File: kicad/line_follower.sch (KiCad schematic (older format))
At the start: 40 parts, among them Q1 ALS-PT19-315C_L177_TR8, Q2 ALS-PT19-315C_L177_TR8, Q3 ALS-PT19-315C_L177_TR8, Q4 ALS-PT19-315C_L177_TR8, Q5 ALS-PT19-315C_L177_TR8, SW1 SW_Push, U1 A4950E, U2 A4950E, U3 NCV4274CDT50RKG, X1 ESP32_DEVKITV1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

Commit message: Board: Almost complete schematic, rough layout of pcb
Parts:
- removed Q1, Q2, Q3, Q4, Q5: ALS-PT19-315C_L177_TR8, line_follower:PHOTOTRANSISTOR-1.7MM, symbol line_follower-eagle-import:ALS-PT19-315C_L177_TR8
- added Q2, Q3, Q4, Q5: ALS-PT19-315C_L177_TR8, cube-library:phototransistor-1.7mm, symbol Device:Q_Photo_NPN
- C8, C9: renamed from C?; footprint (none) -> Capacitor_SMD:CP_Elec_6.3x5.8
- M1, M2: renamed from M?; footprint (none) -> cube-library:SolderWirePad1x6_p2.54
- Q1: renamed from Q?; value Q_Photo_NPN -> ALS-PT19-315C_L177_TR8; footprint (none) -> cube-library:phototransistor-1.7mm
- SW1: footprint (none) -> cube-library:4.5mm_tact_switch
- U1, U2: footprint Package_SO:SOIC-8-1EP_3.9x4.9mm_P1.27mm_EP2.41x3.3mm -> cube-library:SOIC-8-1EP_3.9x4.9mm_P1.27mm_EP2.41x3.3mm_HandSolder
- X1: footprint esp32_devkitv1:ESP32_DEVKITV1 -> cube-library:ESP32_DEVKITV1
- X3: footprint (none) -> cube-library:SolderWirePad1x3_p2.54
- gave numbers to parts that had none: 14
- renumbered R1 to R6, R2 to R7
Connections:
- net labels removed: VBAT
- no-connect marks 0 -> 7
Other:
- note added: "EN has internal pull up"
- note added: "Line sensor LEDs\n\nCharlieplexing leds, using ESP32 GPIO drive strength to limit current.\nShould be safe even at max drive strength at about 30mA per LED.\n\nSee https://www.esp32.com/viewtopic.php?f=12&t=5840#p25550"
- note added: "Power supply:\n\nBoth ESP32-DEVKITV1 and GY-521 have on board 3.3V regulators.\nWe're using the one on ESP32 to power small stuff around the board.\n\nNCV4274CDT low dropout voltage regulator was chosen because it\nhas low enough dropout voltage to power the board from 2S LiPo,\nand has an internal diode in series, so that back powering the board\nfrom USB is safe (Powers everything except the mo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"
- note added: "Secondary I2C is not used"
- note removed: "Line sensor LEDs\n\nCharlieplexing leds, using ESP32 GPIO drive strength to limit current.\nShould be fairly safe even at max drive strength at about 30mA per LED.\n\nSee https://www.esp32.com/viewtopic.php?f=12&t=5840#p25550"
- note removed: "Power supply:\n\nBoth ESP32-DEVKITV1 and GY-521 have on board 3.3V regulators.\nWe're using the one on ESP32 to power small stuff around the board."
- moved on the sheet: C1, C10, C11, C2, C3, C4, C5, C6, C7, C8, C9, D1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

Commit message: Getting there with the PCB design.
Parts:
- added HS1, HS2, HS3, HS4: Heatsink_Pad, cube-library:3x3_thermal_vias, symbol Mechanical:Heatsink_Pad
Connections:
- net +3V3: now also U1.4 (VREF), U2.4 (VREF)
- net +5V: no longer U1.4 (VREF), U2.4 (VREF)
- net ENCODER1A: now also X1.21 (RX2); no longer X1.3 (VN)
- net ENCODER1B: now also X1.22 (TX2); no longer X1.2 (VP)
- net ENCODER2A: now also X1.2 (VP); no longer X1.22 (TX2)
- net ENCODER2B: now also X1.3 (VN); no longer X1.21 (RX2)
- net GND: now also HS1.1, HS2.1, HS3.1, HS4.1
- net LINE_LED0: now also X1.10 (D27); no longer X1.8 (D25)
- net LINE_LED1: now also X1.8 (D25); no longer X1.9 (D26)
- net LINE_LED2: now also X1.9 (D26); no longer X1.10 (D27)
- net LINE_SENSOR0: now also X1.7 (D33); no longer X1.4 (D34)
- net LINE_SENSOR3: now also X1.5 (D35); no longer X1.11 (D14)
- net LINE_SENSOR4: now also X1.4 (D34); no longer X1.7 (D33)
- net MOTOR1A: now also X1.13 (D13); no longer X1.25 (D19)
- net MOTOR1B: now also X1.12 (D12); no longer X1.30 (D23)
- net MOTOR2A: now also X1.30 (D23); no longer X1.12 (D12)
- net MOTOR2B: now also X1.25 (D19); no longer X1.13 (D13)
- net RANGE: now also X1.11 (D14); no longer X1.5 (D35)
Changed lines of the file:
@@
 	550  1450 1350 1450
 Text Label 550  1450 0    70   ~ 0
-LINE_LED0
+LINE_LED1
 Wire Wire Line
 	1350 1550 550  1550
 Text Label 550  1550 0    70   ~ 0
-LINE_LED1
+LINE_LED2
 Wire Wire Line
 	1350 1650 550  1650
 Text Label 550  1650 0    70   ~ 0
-LINE_LED2
+LINE_LED0
 Wire Wire Line
 	1350 1850 550  1850
 Text Label 550  1850 0    70   ~ 0
-MOTOR2A
+MOTOR1B
 Wire Wire Line
 	2450 2150 2550 2150
@@
 	1350 1950 550  1950
 Text Label 550  1950 0    70   ~ 0
-MOTOR2B
+MOTOR1A
 Wire Wire Line
 	2450 750  3250 750
 Text Label 3250 750  2    70   ~ 0
-MOTOR1B
+MOTOR2A
 Wire Wire Line
 	2450 1250 3250 1250
 Text Label 3250 1250 2    70   ~ 0
-MOTOR1A
+MOTOR2B
 Text Label 1000 4700 0    70   ~ 0
 BUTTON
@@
 	1350 1150 550  1150
 Text Label 550  1150 0    70   ~ 0
-RANGE
+LINE_SENSOR3
 Wire Wire Line
 	1000 7000 1200 7000
@@
 	550  1350 1350 1350
 Text Label 550  1350 0    70   ~ 0
-LINE_SENSOR4
+LINE_SENSOR0
 Wire Wire Line
 	550  1750 1350 1750
 Text Label 550  1750 0    70   ~ 0
-LINE_SENSOR3
+RANGE
 Wire Wire Line
 	550  1250 1350 1250
@@
 	550  1050 1350 1050
 Text Label 550  1050 0    70   ~ 0
-LINE_SENSOR0
+LINE_SENSOR4
 Wire Wire Line
 	1350 850  550  850
 Text Label 550  850  0    70   ~ 0
-ENCODER1B
+ENCODER2A
 Wire Wire Line
 	1350 950  550  950
 Text Label 550  950  0    70   ~ 0
-ENCODER1A
+ENCODER2B
 Wire Wire Line
 	2450 1550 3250 1550
 Text Label 3250 1550 2    70   ~ 0
-ENCODER2A
+ENCODER1B
 Wire Wire Line
 	2450 1650 3250 1650
 Text Label 3250 1650 2    70   ~ 0
-ENCODER2B
+ENCODER1A
 Wire Wire Line
 	1500 3200 800  3200
@@
 $EndComp
 $Comp
-L power:+5V #PWR0104
-U 1 1 5F6B266B
-P 4750 6950
-F 0 "#PWR0104" H 4750 6800 50  0001 C CNN
-F 1 "+5V" V 4765 7078 50  0000 L CNN
-F 2 "" H 4750 6950 50  0001 C CNN
-F 3 "" H 4750 6950 50  0001 C CNN
-	1    4750 6950
-	0    -1   -1   0
-$EndComp
-$Comp
 L cube-library:MOTOR_ENC M2
 U 1 1 5F092189
@@
 $EndComp
 $Comp
-L power:+5V #PWR0103
-U 1 1 5F6B001E
-P 4750 4250
-F 0 "#PWR0103" H 4750 4100 50  0001 C CNN
-F 1 "+5V" V 4765 4378 50  0000 L CNN
-F 2 "" H 4750 4250 50  0001 C CNN
-F 3 "" H 4750 4250 50  0001 C CNN
-	1    4750 4250
-	0    -1   -1   0
-$EndComp
-$Comp
 L cube-library:MOTOR_ENC M1
 U 1 1 5F08FA5D
@@
 Wire Wire Line
 	5250 4650 5250 4800
-Wire Wire Line
-	5250 4650 5250 4550
 Connection ~ 5250 4650
 Wire Wire Line
@@
 Wire Wire Line
 	9850 4200 10050 4200
+$Comp
+L Mechanical:Heatsink_Pad HS1
+U 1 1 5F1F9B2A
+P 6750 3050
+F 0 "HS1" H 6891 3089 50  0000 L CNN
+F 1 "Heatsink_Pad" H 6891 2998 50  0000 L CNN
+F 2 "cube-library:3x3_thermal_vias" H 6762 3000 50  0001 C CNN
+F 3 "~" H 6762 3000 50  0001 C CNN
+	1    6750 3050
+	1    0    0    -1
+$EndComp
+$Comp
+L Mechanical:Heatsink_Pad HS2
+U 1 1 5F204F60
+P 6750 3550
+F 0 "HS2" H 6891 3589 50  0000 L CNN
+F 1 "Heatsink_Pad" H 6891 3498 50  0000 L CNN
+F 2 "cube-library:3x3_thermal_vias" H 6762 3500 50  0001 C CNN
+F 3 "~" H 6762 3500 50  0001 C CNN
+	1    6750 3550
+	1    0    0    -1
+$EndComp
+Wire Wire Line
+	5250 4650 5250 4550
+$Comp
+L power:GND #PWR0127
+U 1 1 5F2722C1
+P 6750 3150
+F 0 "#PWR0127" H 6750 2900 50  0001 C CNN
+F 1 "GND" H 6755 2977 50  0000 C CNN
+F 2 "" H 6750 3150 50  0001 C CNN
+F 3 "" H 6750 3150 50  0001 C CNN
+	1    6750 3150
+	1    0    0    -1
+$EndComp
+$Comp
+L power:GND #PWR0128
+U 1 1 5F27922E
+P 6750 3650
+F 0 "#PWR0128" H 6750 3400 50  0001 C CNN
+F 1 "GND" H 6755 3477 50  0000 C CNN
+F 2 "" H 6750 3650 50  0001 C CNN
+F 3 "" H 6750 3650 50  0001 C CNN
+	1    6750 3650
+	1    0    0    -1
+$EndComp
+$Comp
+L Mechanical:Heatsink_Pad HS3
+U 1 1 5F292D49
+P 6700 5750
+F 0 "HS3" H 6841 5789 50  0000 L CNN
+F 1 "Heatsink_Pad" H 6841 5698 50  0000 L CNN
+F 2 "cube-library:3x3_thermal_vias" H 6712 5700 50  0001 C CNN
+F 3 "~" H 6712 5700 50  0001 C CNN
+	1    6700 5750
+	1    0    0    -1
+$EndComp
+$Comp
+L Mechanical:Heatsink_Pad HS4
+U 1 1 5F29358A
+P 6700 6250
+F 0 "HS4" H 6841 6289 50  0000 L CNN
+F 1 "Heatsink_Pad" H 6841 6198 50  0000 L CNN
+F 2 "cube-library:3x3_thermal_vias" H 6712 6200 50  0001 C CNN
+F 3 "~" H 6712 6200 50  0001 C CNN
+	1    6700 6250
+	1    0    0    -1
+$EndComp
+$Comp
+L power:GND #PWR0129
+U 1 1 5F29604C
+P 6700 6350
+F 0 "#PWR0129" H 6700 6100 50  0001 C CNN
+F 1 "GND" H 6705 6177 50  0000 C CNN
+F 2 "" H 6700 6350 50  0001 C CNN
+F 3 "" H 6700 6350 50  0001 C CNN
+	1    6700 6350
+	1    0    0    -1
+$EndComp
+$Comp
+L power:GND #PWR0130
+U 1 1 5F29648E
+P 6700 5850
+F 0 "#PWR0130" H 6700 5600 50  0001 C CNN
+F 1 "GND" H 6705 5677 50  0000 C CNN
+F 2 "" H 6700 5850 50  0001 C CNN
+F 3 "" H 6700 5850 50  0001 C CNN
+	1    6700 5850
+	1    0    0    -1
+$EndComp
+$Comp
+L power:+3.3V #PWR?
+U 1 1 5F2EDDA3
+P 4750 4250
+F 0 "#PWR?" H 4750 4100 50  0001 C CNN
+F 1 "+3.3V" V 4765 4378 50  0000 L CNN
+F 2 "" H 4750 4250 50  0001 C CNN
+F 3 "" H 4750 4250 50  0001 C CNN
+	1    4750 4250
+	0    -1   -1   0
+$EndComp
+$Comp
+L power:+3.3V #PWR?
+U 1 1 5F2F0575
+P 4750 6950
+F 0 "#PWR?" H 4750 6800 50  0001 C CNN
+F 1 "+3.3V" V 4765 7078 50  0000 L CNN
+F 2 "" H 4750 6950 50  0001 C CNN
+F 3 "" H 4750 6950 50  0001 C CNN
+	1    4750 6950
+	0    -1   -1   0
+$EndComp
 $EndSCHEMATC

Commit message: Board done except for the motor mounts
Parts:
- added H1, H2, H3, H4, H5: MountingHole, MountingHole:MountingHole_3.2mm_M3, symbol Mechanical:MountingHole
- M1, M2: footprint cube-library:SolderWirePad1x6_p2.54 -> cube-library:SolderWirePad2x3_p2.54_staggered
- renumbered HS4 to HS2, HS2 to HS4
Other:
- note added: "H bridges:\n\nWe are not using current limiting,\n3.3V is just tied to VREF because it was close for routing"
- note added: "UART TX/RX\nconnected to USB"
- note added: "has internal pull up"
- note added: "on-board LED"
- note removed: "EN has internal pull up"
- note removed: "GPIO1 & 3 are UART TX/RX connected to USB"
- note removed: "GPIO2 has the on-board LED"
- note removed: "H bridges:\n\nWe are not using current limiting,\n5V is just tied to VREF because it was close for routing"
- moved on the sheet: C1, C10, C11, C2, C3, C4, C5, C6, C7, C8, C9, D1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

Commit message: Small PCB tweaks
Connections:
- net GND: now also J1.3 (Attach1), J1.4 (Attach2)
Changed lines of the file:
@@
 	1300 6800 1500 6800
 Wire Wire Line
-	1500 6800 1500 7300
+	1500 6800 1500 6950
 Wire Wire Line
 	1800 7200 1800 7300
@@
 	1    2000 1450
 	1    0    0    -1
-$EndComp
-$Comp
-L cube-library:XT30PW-M J1
-U 1 1 5EDD27F3
-P 1100 6550
-F 0 "J1" H 1163 6625 50  0000 C CNN
-F 1 "XT30PW-M" H 1163 6534 50  0000 C CNN
-F 2 "cube-library:XT30PW-M" H 1200 5900 50  0001 C CNN
-F 3 "https://www.tme.eu/Document/ce4077e36b79046da520ca73227e15de/XT30PW%20SPEC.pdf" H 1100 6550 50  0001 C CNN
-	1    1100 6550
-	-1   0    0    -1
 $EndComp
 $Comp
@@
 	1    0    0    -1
 $EndComp
+$Comp
+L cube-library:XT30PW-M J1
+U 1 1 5EDD27F3
+P 1100 6550
+F 0 "J1" H 1163 6625 50  0000 C CNN
+F 1 "XT30PW-M" H 1163 6534 50  0000 C CNN
+F 2 "cube-library:XT30PW-M" H 1200 5900 50  0001 C CNN
+F 3 "https://www.tme.eu/Document/ce4077e36b79046da520ca73227e15de/XT30PW%20SPEC.pdf" H 1100 6550 50  0001 C CNN
+	1    1100 6550
+	-1   0    0    -1
+$EndComp
+Wire Wire Line
+	1300 6950 1500 6950
+Connection ~ 1500 6950
+Wire Wire Line
+	1500 6950 1500 7050
+Wire Wire Line
+	1300 7050 1500 7050
+Connection ~ 1500 7050
+Wire Wire Line
+	1500 7050 1500 7300
 $EndSCHEMATC

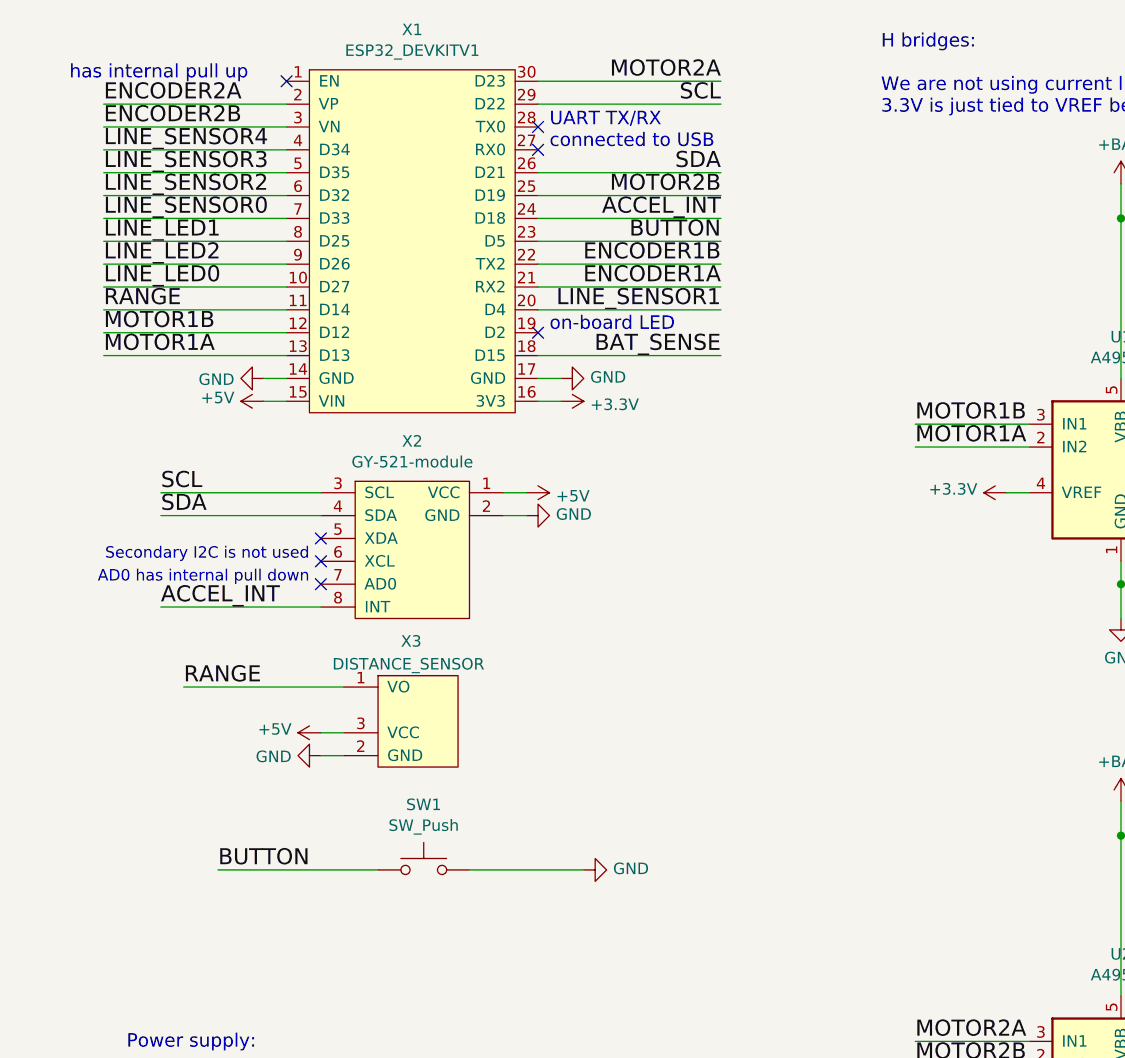
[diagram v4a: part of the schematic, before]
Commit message: Untangled routing at the front of the robot a bit, moved battery location
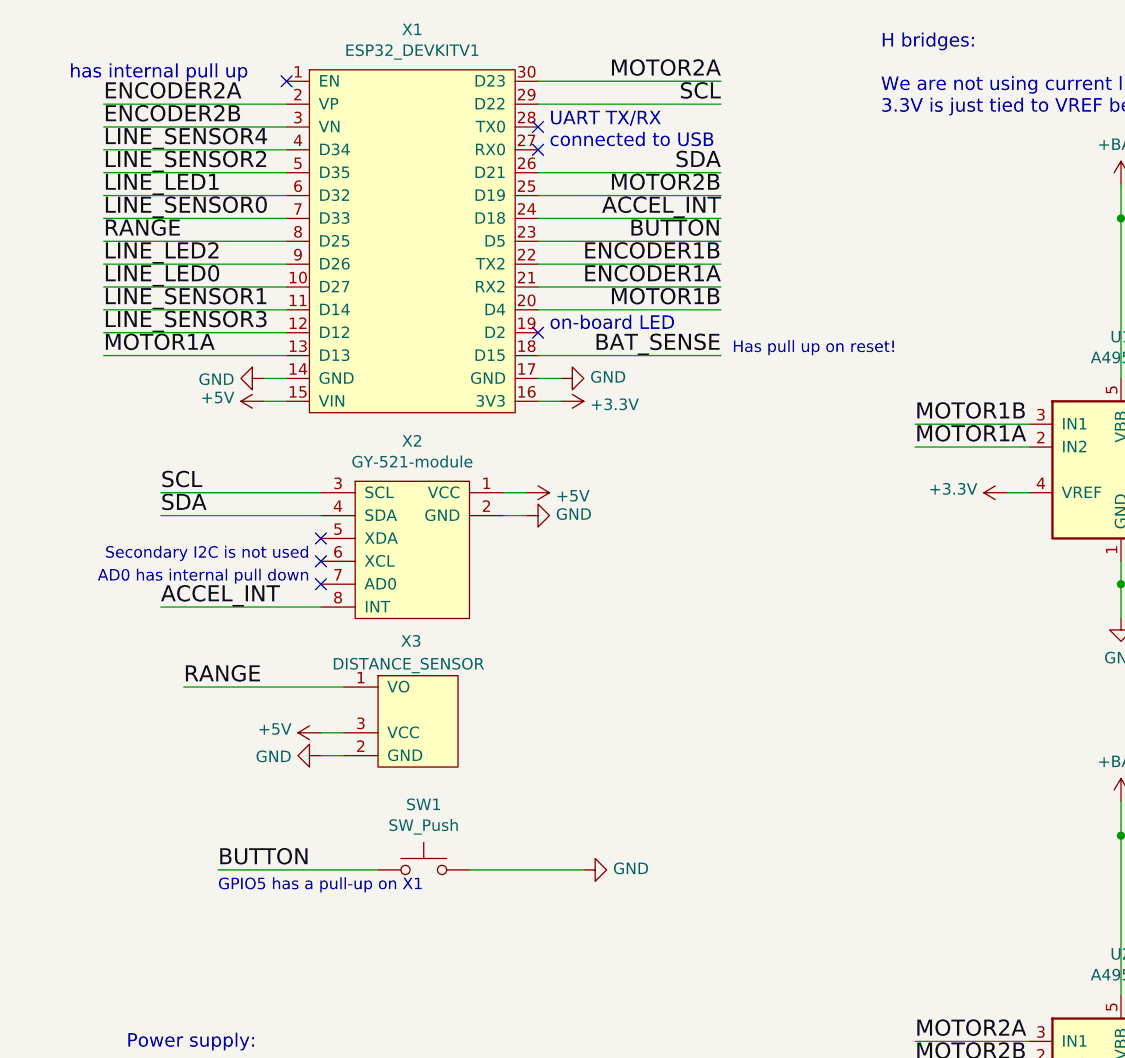
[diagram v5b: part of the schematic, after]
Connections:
- net LINE_LED1: now also X1.6 (D32); no longer X1.8 (D25)
- net LINE_SENSOR1: now also X1.11 (D14); no longer X1.20 (D4)
- net LINE_SENSOR2: now also X1.5 (D35); no longer X1.6 (D32)
- net LINE_SENSOR3: now also X1.12 (D12); no longer X1.5 (D35)
- net MOTOR1B: now also X1.20 (D4); no longer X1.12 (D12)
- net RANGE: now also X1.8 (D25); no longer X1.11 (D14)
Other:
- note added: "GPIO5 has a pull-up on X1"
- note added: "Has pull up on reset!"
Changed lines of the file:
@@
 	650  1450 1450 1450
 Text Label 650  1450 0    70   ~ 0
-LINE_LED1
+RANGE
 Wire Wire Line
 	1450 1550 650  1550
@@
 	1450 1850 650  1850
 Text Label 650  1850 0    70   ~ 0
-MOTOR1B
+LINE_SENSOR3
 Wire Wire Line
 	2550 2150 2650 2150
@@
 	1450 1150 650  1150
 Text Label 650  1150 0    70   ~ 0
-LINE_SENSOR3
+LINE_SENSOR2
 Wire Wire Line
 	1300 6700 1500 6700
@@
 	650  1750 1450 1750
 Text Label 650  1750 0    70   ~ 0
-RANGE
+LINE_SENSOR1
 Wire Wire Line
 	650  1250 1450 1250
 Text Label 650  1250 0    70   ~ 0
-LINE_SENSOR2
+LINE_LED1
 Wire Wire Line
 	3350 1750 2550 1750
 Text Label 3350 1750 2    70   ~ 0
-LINE_SENSOR1
+MOTOR1B
 Wire Wire Line
 	650  1050 1450 1050
@@
 Wire Wire Line
 	1500 7050 1500 7300
+Text Notes 1150 4300 0    50   ~ 0
+GPIO5 has a pull-up on X1
+Text Notes 3400 1950 0    50   ~ 0
+Has pull up on reset!
 $EndSCHEMATC

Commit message: board: A bit more tweaking
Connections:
- net LINE_SENSOR3: now also X1.8 (D25); no longer X1.12 (D12)
- net RANGE: now also X1.12 (D12); no longer X1.8 (D25)
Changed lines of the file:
@@
 Wire Wire Line
 	650  1450 1450 1450
-Text Label 650  1450 0    70   ~ 0
-RANGE
 Wire Wire Line
 	1450 1550 650  1550
@@
 Wire Wire Line
 	1450 1850 650  1850
-Text Label 650  1850 0    70   ~ 0
-LINE_SENSOR3
 Wire Wire Line
 	2550 2150 2650 2150
@@
 Wire Wire Line
 	650  1350 1450 1350
-Text Label 650  1350 0    70   ~ 0
-LINE_SENSOR0
 Wire Wire Line
 	650  1750 1450 1750
@@
 Wire Wire Line
 	650  1250 1450 1250
-Text Label 650  1250 0    70   ~ 0
-LINE_LED1
 Wire Wire Line
 	3350 1750 2550 1750
@@
 $EndComp
 $Comp
-L Device:C C5
-U 1 1 5F8649E1
-P 9900 4400
-F 0 "C5" V 9648 4400 50  0000 C CNN
-F 1 "100nF" V 9739 4400 50  0000 C CNN
-F 2 "Capacitor_SMD:C_0805_2012Metric_Pad1.15x1.40mm_HandSolder" H 9938 4250 50  0001 C CNN
-F 3 "~" H 9900 4400 50  0001 C CNN
-	1    9900 4400
-	0    1    1    0
-$EndComp
-$Comp
-L Device:C C4
-U 1 1 5F864455
-P 9900 3600
-F 0 "C4" V 9648 3600 50  0000 C CNN
-F 1 "100nF" V 9739 3600 50  0000 C CNN
-F 2 "Capacitor_SMD:C_0805_2012Metric_Pad1.15x1.40mm_HandSolder" H 9938 3450 50  0001 C CNN
-F 3 "~" H 9900 3600 50  0001 C CNN
-	1    9900 3600
-	0    1    1    0
-$EndComp
-$Comp
-L Device:C C3
-U 1 1 5F863E50
-P 9900 2800
-F 0 "C3" V 9648 2800 50  0000 C CNN
-F 1 "100nF" V 9739 2800 50  0000 C CNN
-F 2 "Capacitor_SMD:C_0805_2012Metric_Pad1.15x1.40mm_HandSolder" H 9938 2650 50  0001 C CNN
-F 3 "~" H 9900 2800 50  0001 C CNN
-	1    9900 2800
-	0    1    1    0
-$EndComp
-$Comp
-L Device:C C2
-U 1 1 5F863769
-P 9900 2000
-F 0 "C2" V 9648 2000 50  0000 C CNN
-F 1 "100nF" V 9739 2000 50  0000 C CNN
-F 2 "Capacitor_SMD:C_0805_2012Metric_Pad1.15x1.40mm_HandSolder" H 9938 1850 50  0001 C CNN
-F 3 "~" H 9900 2000 50  0001 C CNN
-	1    9900 2000
-	0    1    1    0
-$EndComp
-$Comp
-L Device:C C1
-U 1 1 5F862D5E
-P 9900 1200
-F 0 "C1" V 9648 1200 50  0000 C CNN
-F 1 "100nF" V 9739 1200 50  0000 C CNN
-F 2 "Capacitor_SMD:C_0805_2012Metric_Pad1.15x1.40mm_HandSolder" H 9938 1050 50  0001 C CNN
-F 3 "~" H 9900 1200 50  0001 C CNN
-	1    9900 1200
-	0    1    1    0
-$EndComp
-$Comp
 L Device:R R5
 U 1 1 5F810985
@@
 F 3 "~" H 9900 3400 50  0001 C CNN
 	1    9900 3400
-	0    1    1    0
-$EndComp
-$Comp
-L Device:R R3
-U 1 1 5F8100EF
-P 9900 2600
-F 0 "R3" V 9693 2600 50  0000 C CNN
-F 1 "5k6" V 9784 2600 50  0000 C CNN
-F 2 "Resistor_SMD:R_0805_2012Metric_Pad1.15x1.40mm_HandSolder" V 9830 2600 50  0001 C CNN
-F 3 "~" H 9900 2600 50  0001 C CNN
-	1    9900 2600
 	0    1    1    0
 $EndComp
@@
 Text Notes 3400 1950 0    50   ~ 0
 Has pull up on reset!
+Text Label 650  1350 0    70   ~ 0
+LINE_SENSOR0
+Text Label 650  1250 0    70   ~ 0
+LINE_LED1
+$Comp
+L Device:R R3
+U 1 1 5F8100EF
+P 9900 2600
+F 0 "R3" V 9693 2600 50  0000 C CNN
+F 1 "5k6" V 9784 2600 50  0000 C CNN
+F 2 "Resistor_SMD:R_0805_2012Metric_Pad1.15x1.40mm_HandSolder" V 9830 2600 50  0001 C CNN
+F 3 "~" H 9900 2600 50  0001 C CNN
+	1    9900 2600
+	0    1    1    0
+$EndComp
+Text Label 650  1450 0    70   ~ 0
+LINE_SENSOR3
+$Comp
+L Device:C C5
+U 1 1 5F8649E1
+P 9900 4400
+F 0 "C5" V 9648 4400 50  0000 C CNN
+F 1 "100nF" V 9739 4400 50  0000 C CNN
+F 2 "Capacitor_SMD:C_0805_2012Metric_Pad1.15x1.40mm_HandSolder" H 9938 4250 50  0001 C CNN
+F 3 "~" H 9900 4400 50  0001 C CNN
+	1    9900 4400
+	0    1    1    0
+$EndComp
+$Comp
+L Device:C C4
+U 1 1 5F864455
+P 9900 3600
+F 0 "C4" V 9648 3600 50  0000 C CNN
+F 1 "100nF" V 9739 3600 50  0000 C CNN
+F 2 "Capacitor_SMD:C_0805_2012Metric_Pad1.15x1.40mm_HandSolder" H 9938 3450 50  0001 C CNN
+F 3 "~" H 9900 3600 50  0001 C CNN
+	1    9900 3600
+	0    1    1    0
+$EndComp
+$Comp
+L Device:C C3
+U 1 1 5F863E50
+P 9900 2800
+F 0 "C3" V 9648 2800 50  0000 C CNN
+F 1 "100nF" V 9739 2800 50  0000 C CNN
+F 2 "Capacitor_SMD:C_0805_2012Metric_Pad1.15x1.40mm_HandSolder" H 9938 2650 50  0001 C CNN
+F 3 "~" H 9900 2800 50  0001 C CNN
+	1    9900 2800
+	0    1    1    0
+$EndComp
+$Comp
+L Device:C C2
+U 1 1 5F863769
+P 9900 2000
+F 0 "C2" V 9648 2000 50  0000 C CNN
+F 1 "100nF" V 9739 2000 50  0000 C CNN
+F 2 "Capacitor_SMD:C_0805_2012Metric_Pad1.15x1.40mm_HandSolder" H 9938 1850 50  0001 C CNN
+F 3 "~" H 9900 2000 50  0001 C CNN
+	1    9900 2000
+	0    1    1    0
+$EndComp
+$Comp
+L Device:C C1
+U 1 1 5F862D5E
+P 9900 1200
+F 0 "C1" V 9648 1200 50  0000 C CNN
+F 1 "100nF" V 9739 1200 50  0000 C CNN
+F 2 "Capacitor_SMD:C_0805_2012Metric_Pad1.15x1.40mm_HandSolder" H 9938 1050 50  0001 C CNN
+F 3 "~" H 9900 1200 50  0001 C CNN
+	1    9900 1200
+	0    1    1    0
+$EndComp
+Text Label 650  1850 0    70   ~ 0
+RANGE
 $EndSCHEMATC
